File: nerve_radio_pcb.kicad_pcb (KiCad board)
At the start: 4 copper layers, 50 x 50 mm, 11 parts, among them J1 BF030-20A-B1-0360-0277-0600-LB, J2 5V GPIO Breakout, J3 3V SPI Breakout, U1 XBP9B-DMWT-002, U2 TXB0104QPWRQ1

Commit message: Update config.kibot.yaml, cleanup, add fiducials
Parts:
- added FM1: 1mm, Fiducial:Fiducial_1mm_Mask2mm, F.Cu at (133.5, 86.2)
- added FM2: 1mm, Fiducial:Fiducial_1mm_Mask2mm, F.Cu at (133.5, 123.8)
- added FM3: 1mm, Fiducial:Fiducial_1mm_Mask2mm, F.Cu at (163.5, 123.8)
- added FM4: 1mm, Fiducial:Fiducial_1mm_Mask2mm, B.Cu at (133.5, 86.2)
- added FM5: 1mm, Fiducial:Fiducial_1mm_Mask2mm, B.Cu at (133.5, 123.8)
- added FM6: 1mm, Fiducial:Fiducial_1mm_Mask2mm, B.Cu at (163.5, 123.8)

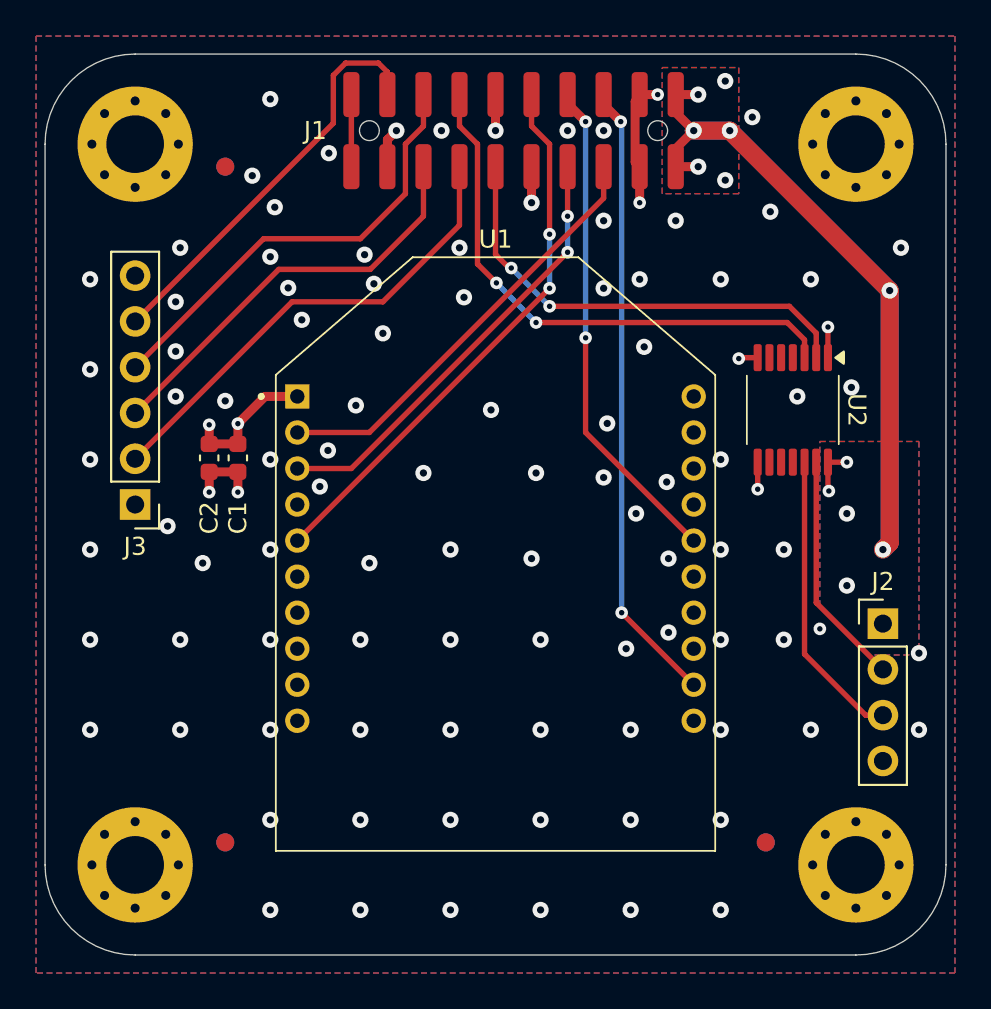
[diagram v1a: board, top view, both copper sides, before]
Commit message: Update component_library and add 5V buck
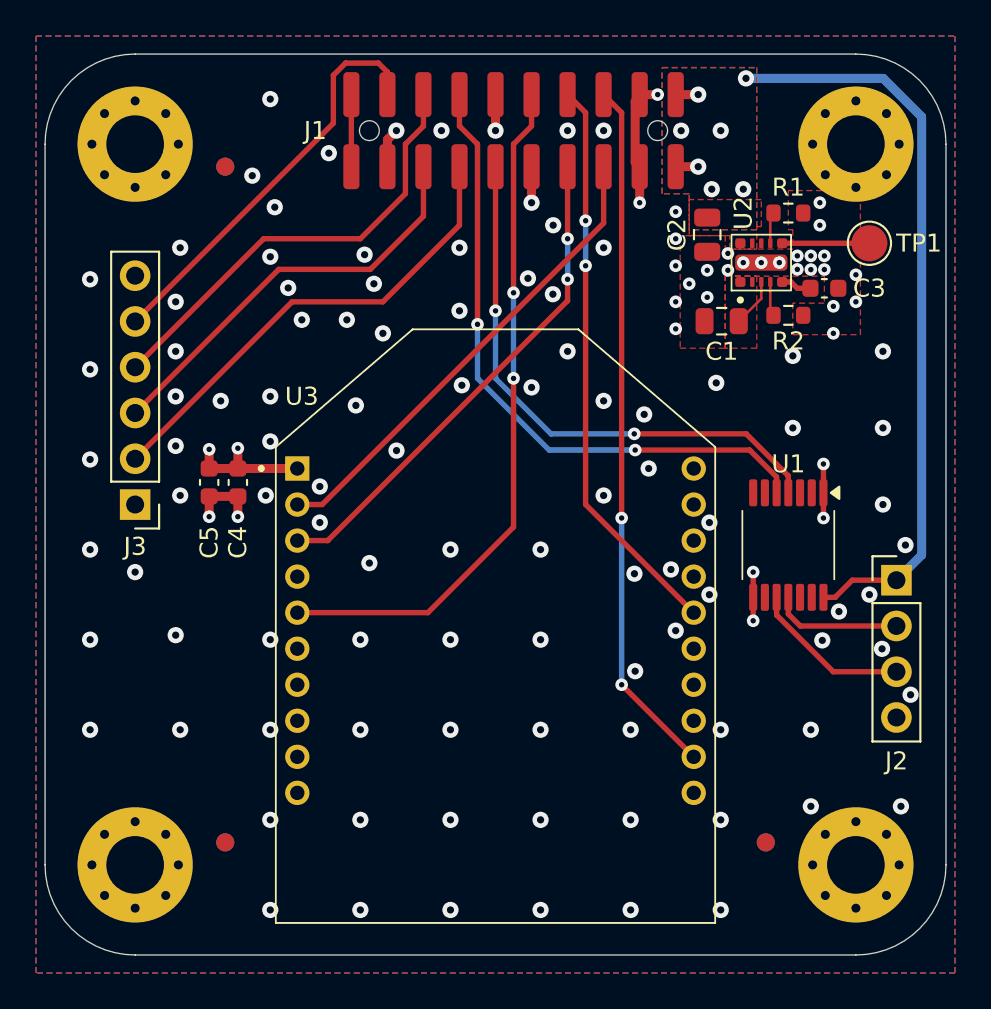
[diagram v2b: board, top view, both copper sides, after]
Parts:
- added C1: 10u, Capacitor_SMD:C_0805_2012Metric, F.Cu at (161.1, 94.8)
- added C2: 22u, Capacitor_SMD:C_0805_2012Metric, F.Cu at (160.2, 90.0)
- added C3: 16n, Capacitor_SMD:C_0603_1608Metric, F.Cu at (166.8, 93.0)
- added R1: 76k8, Resistor_SMD:R_0603_1608Metric, F.Cu at (164.8, 88.8)
- added R2: 76k8, Resistor_SMD:R_0603_1608Metric, F.Cu at (164.8, 94.5)
- added TP1: TestPoint, TestPoint:TestPoint_Pad_D2.0mm, F.Cu at (169.2, 90.5)
- added U2: TPSM82903, ti_buck:tpsm8290x, F.Cu at (163.2, 91.6)
- moved U1 7.50 mm to (164.8, 107.2)
- moved U3 4.00 mm to (148.5, 111.8)
- moved J2 2.52 mm to (170.8, 109.2)
- moved C4 1.36 mm to (134.2, 103.8)
- moved C5 1.36 mm to (132.6, 103.8)
- renumbered C1 to C4, C2 to C5, U2 to U1, U1 to U3
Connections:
- U1 pad 10: unconnected-(U2-B4-Pad10) -> /GPIO_2/PWM_2_{5V}
- U1 pad 11: unconnected-(U2-B3-Pad11) -> /GPIO_1/PWM_1_{5V}
- U1 pad 12: /GPIO_2/PWM_2_{5V} -> unconnected-(U1-B2-Pad12)
- U1 pad 13: /GPIO_1/PWM_1_{5V} -> unconnected-(U1-B1-Pad13)
- U1 pad 2: /GPIO_1/PWM_1 -> unconnected-(U1-A1-Pad2)
- U1 pad 3: /GPIO_2/PWM_2 -> unconnected-(U1-A2-Pad3)
- U1 pad 4: unconnected-(U2-A3-Pad4) -> /GPIO_1/PWM_1
- U1 pad 5: unconnected-(U2-A4-Pad5) -> /GPIO_2/PWM_2
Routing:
- net +5V: track 68.2 -> 45.9 mm, vias 12 -> 7
- net /GPIO_2/PWM_2_{5V}: track 16.4 -> 8.94 mm
- net /RADIO_NRST: track 31.0 -> 38.4 mm
- net /GPIO_1/PWM_1_{5V}: track 13.0 -> 7.20 mm
- net /GPIO_1/PWM_1: track 25.8 -> 31.2 mm
- net /GPIO_2/PWM_2: track 30.7 -> 35.9 mm
- net Net-(U2-PG): track 0.00 -> 4.84 mm
- net /RADIO_UART_RTS: track 27.7 -> 31.6 mm
- net /RADIO_UART_CTS: track 34.8 -> 38.8 mm
- net /RADIO_UART_TX: track 24.7 -> 28.0 mm
- net +VSUPPLY: track 0.00 -> 2.69 mm
- net /RADIO_UART_RX: track 24.1 -> 26.6 mm
- net Net-(U2-MODE/S-CONF): track 0.00 -> 1.92 mm
- net +3V3: track 18.1 -> 20.0 mm, vias 6 -> 8
- net Net-(U2-FB/VSET): track 0.00 -> 1.75 mm
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- added copper zone on F.Cu, net +VSUPPLY

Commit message: Cleanup and add missing transfer vias
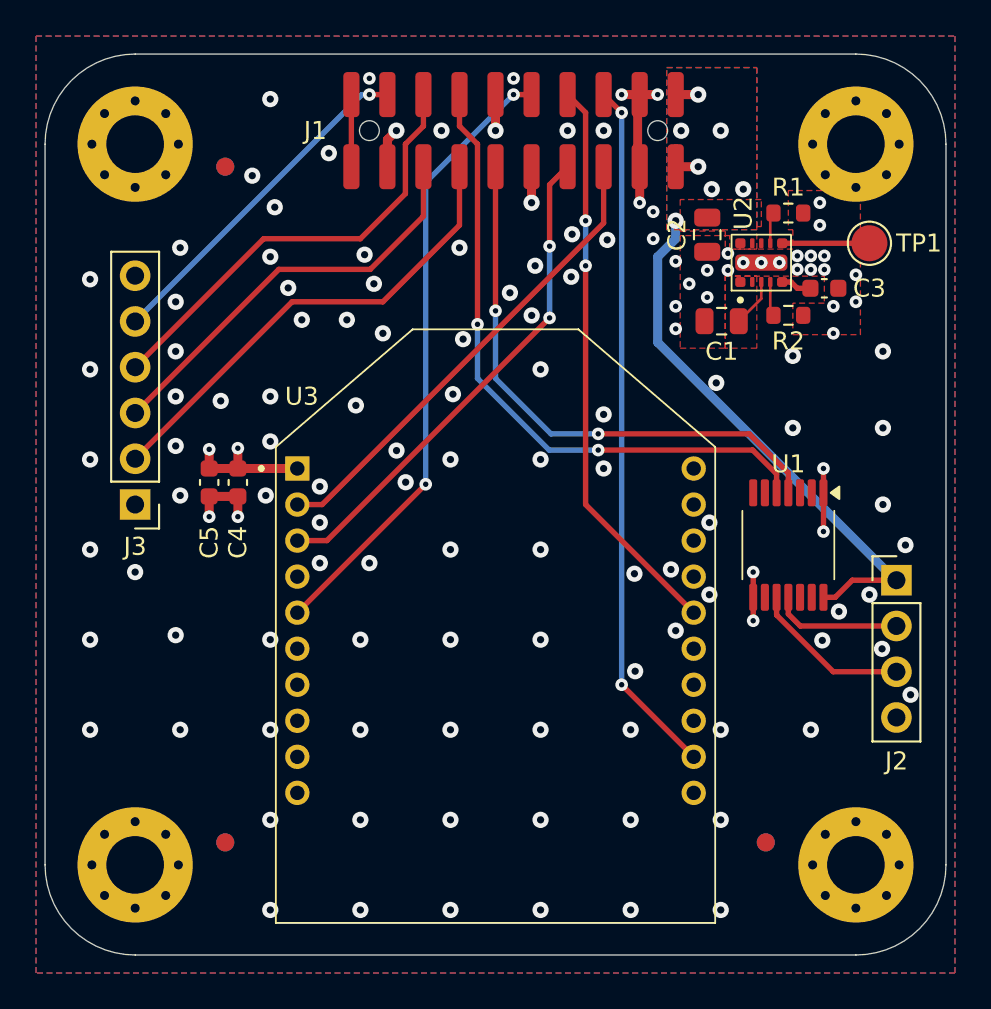
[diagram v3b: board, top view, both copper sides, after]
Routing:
- net +5V: track 45.9 -> 34.8 mm
- net /SPI_CS: track 23.0 -> 19.2 mm, vias 0 -> 1
- net /RADIO_NRST: track 38.4 -> 34.7 mm
- net +3V3: track 20.0 -> 21.5 mm, vias 8 -> 9
- net GND: vias 126 -> 129
